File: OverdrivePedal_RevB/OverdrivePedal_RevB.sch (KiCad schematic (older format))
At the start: 18 parts, among them J1 AudioJack2, J2 Barrel_Jack, J3 Conn_01x03, J5 Conn_01x03, J6 AudioJack2, U2 TL071

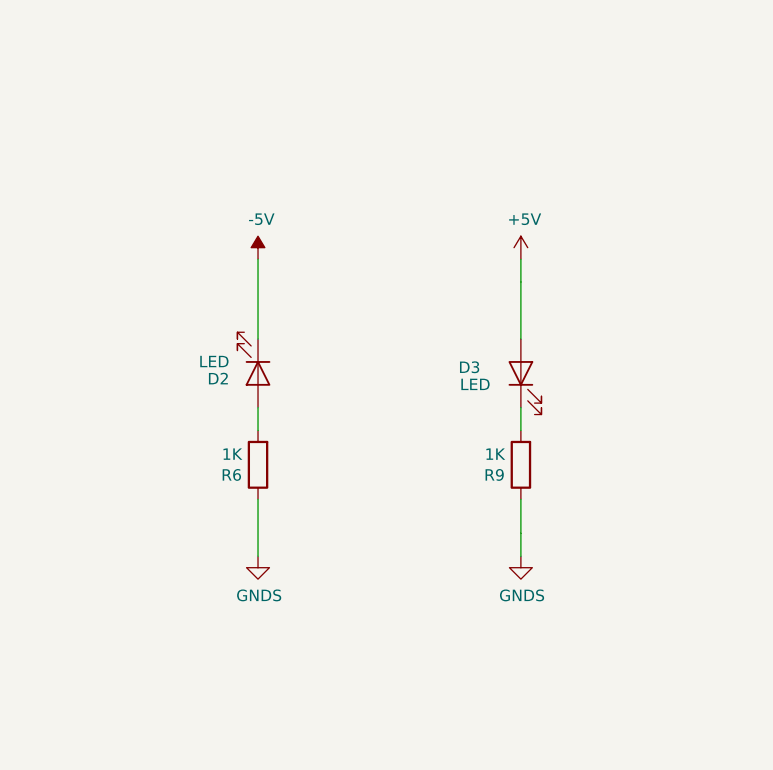
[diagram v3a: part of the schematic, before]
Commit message: Added extra leds
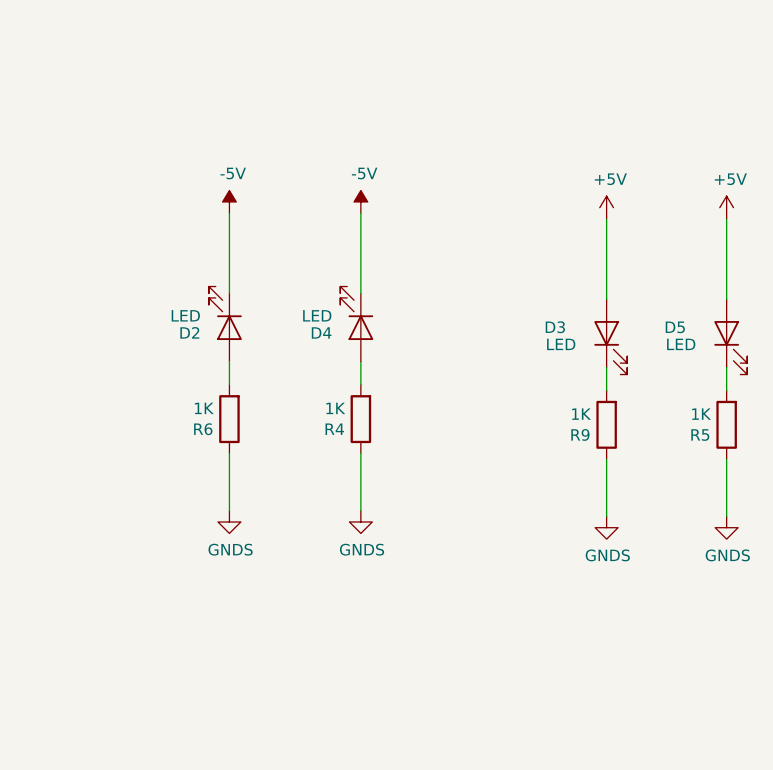
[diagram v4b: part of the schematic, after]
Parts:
- added D4, D5: LED, LED_SMD:LED_1206_3216Metric_Pad1.42x1.75mm_HandSolder, symbol Device:LED
- added R4, R5: 1K, Resistor_SMD:R_0805_2012Metric_Pad1.15x1.40mm_HandSolder, symbol Device:R
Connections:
- wire segments 61 -> 65
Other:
- moved on the sheet: D2, D3, R6, R9
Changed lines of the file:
@@
 L Device:R R9
 U 1 1 5E7266E9
-P 13550 8650
-F 0 "R9" H 13620 8696 50  0000 L CNN
-F 1 "1K" H 13620 8605 50  0000 L CNN
-F 2 "Resistor_SMD:R_0805_2012Metric_Pad1.15x1.40mm_HandSolder" V 13480 8650 50  0001 C CNN
-F 3 "~" H 13550 8650 50  0001 C CNN
-	1    13550 8650
+P 13925 8475
+F 0 "R9" H 13995 8521 50  0000 L CNN
+F 1 "1K" H 13995 8430 50  0000 L CNN
+F 2 "Resistor_SMD:R_0805_2012Metric_Pad1.15x1.40mm_HandSolder" V 13855 8475 50  0001 C CNN
+F 3 "~" H 13925 8475 50  0001 C CNN
+	1    13925 8475
 	-1   0    0    1
 $EndComp
@@
 L Device:R R6
 U 1 1 5E727E16
-P 12400 8650
-F 0 "R6" H 12470 8696 50  0000 L CNN
-F 1 "1K" H 12470 8605 50  0000 L CNN
-F 2 "Resistor_SMD:R_0805_2012Metric_Pad1.15x1.40mm_HandSolder" V 12330 8650 50  0001 C CNN
-F 3 "~" H 12400 8650 50  0001 C CNN
-	1    12400 8650
-	-1   0    0    1
-$EndComp
-Wire Wire Line
-	13550 8500 13550 8400
-Wire Wire Line
-	12400 8500 12400 8400
-Wire Wire Line
-	13550 8100 13550 7850
-Wire Wire Line
-	12400 8100 12400 7750
+P 12275 8450
+F 0 "R6" H 12345 8496 50  0000 L CNN
+F 1 "1K" H 12345 8405 50  0000 L CNN
+F 2 "Resistor_SMD:R_0805_2012Metric_Pad1.15x1.40mm_HandSolder" V 12205 8450 50  0001 C CNN
+F 3 "~" H 12275 8450 50  0001 C CNN
+	1    12275 8450
+	-1   0    0    1
+$EndComp
+Wire Wire Line
+	13925 8325 13925 8225
+Wire Wire Line
+	12275 8300 12275 8200
+Wire Wire Line
+	12275 7900 12275 7550
 $Comp
 L power:GNDS #PWR0108
 U 1 1 5E73B1FE
-P 13550 9050
-F 0 "#PWR0108" H 13550 8800 50  0001 C CNN
-F 1 "GNDS" H 13555 8877 50  0000 C CNN
-F 2 "" H 13550 9050 50  0001 C CNN
-F 3 "" H 13550 9050 50  0001 C CNN
-	1    13550 9050
+P 13925 8875
+F 0 "#PWR0108" H 13925 8625 50  0001 C CNN
+F 1 "GNDS" H 13930 8702 50  0000 C CNN
+F 2 "" H 13925 8875 50  0001 C CNN
+F 3 "" H 13925 8875 50  0001 C CNN
+	1    13925 8875
 	1    0    0    -1
 $EndComp
@@
 L power:+5V #PWR0109
 U 1 1 5E73B611
-P 13550 7750
-F 0 "#PWR0109" H 13550 7600 50  0001 C CNN
-F 1 "+5V" H 13565 7923 50  0000 C CNN
-F 2 "" H 13550 7750 50  0001 C CNN
-F 3 "" H 13550 7750 50  0001 C CNN
-	1    13550 7750
-	1    0    0    -1
-$EndComp
-Wire Wire Line
-	13550 9050 13550 8950
-Wire Wire Line
-	13550 8950 13550 8800
-Wire Wire Line
-	12400 9050 12400 8800
-Wire Wire Line
-	13550 7750 13550 7850
+P 13925 7575
+F 0 "#PWR0109" H 13925 7425 50  0001 C CNN
+F 1 "+5V" H 13940 7748 50  0000 C CNN
+F 2 "" H 13925 7575 50  0001 C CNN
+F 3 "" H 13925 7575 50  0001 C CNN
+	1    13925 7575
+	1    0    0    -1
+$EndComp
+Wire Wire Line
+	12275 8850 12275 8600
 $Comp
 L Connector:AudioJack2 J1
@@
 L Device:LED D2
 U 1 1 5EFC7770
-P 12400 8250
-F 0 "D2" V 12425 8125 50  0000 R CNN
-F 1 "LED" V 12350 8125 50  0000 R CNN
-F 2 "LED_SMD:LED_1206_3216Metric_Pad1.42x1.75mm_HandSolder" H 12400 8250 50  0001 C CNN
-F 3 "~" H 12400 8250 50  0001 C CNN
-	1    12400 8250
+P 12275 8050
+F 0 "D2" V 12300 7925 50  0000 R CNN
+F 1 "LED" V 12225 7925 50  0000 R CNN
+F 2 "LED_SMD:LED_1206_3216Metric_Pad1.42x1.75mm_HandSolder" H 12275 8050 50  0001 C CNN
+F 3 "~" H 12275 8050 50  0001 C CNN
+	1    12275 8050
 	0    1    1    0
 $EndComp
@@
 L Device:LED D3
 U 1 1 5EFC98F4
-P 13550 8250
-F 0 "D3" V 13575 8475 50  0000 C CNN
-F 1 "LED" V 13500 8450 50  0000 C CNN
-F 2 "LED_SMD:LED_1206_3216Metric_Pad1.42x1.75mm_HandSolder" H 13550 8250 50  0001 C CNN
-F 3 "~" H 13550 8250 50  0001 C CNN
-	1    13550 8250
+P 13925 8075
+F 0 "D3" V 13950 8300 50  0000 C CNN
+F 1 "LED" V 13875 8275 50  0000 C CNN
+F 2 "LED_SMD:LED_1206_3216Metric_Pad1.42x1.75mm_HandSolder" H 13925 8075 50  0001 C CNN
+F 3 "~" H 13925 8075 50  0001 C CNN
+	1    13925 8075
 	0    -1   -1   0
 $EndComp
@@
 L power:-5V #PWR0110
 U 1 1 5EFE78DE
-P 12400 7750
-F 0 "#PWR0110" H 12400 7850 50  0001 C CNN
-F 1 "-5V" H 12415 7923 50  0000 C CNN
-F 2 "" H 12400 7750 50  0001 C CNN
-F 3 "" H 12400 7750 50  0001 C CNN
-	1    12400 7750
+P 12275 7550
+F 0 "#PWR0110" H 12275 7650 50  0001 C CNN
+F 1 "-5V" H 12290 7723 50  0000 C CNN
+F 2 "" H 12275 7550 50  0001 C CNN
+F 3 "" H 12275 7550 50  0001 C CNN
+	1    12275 7550
 	1    0    0    -1
 $EndComp
@@
 L power:GNDS #PWR0111
 U 1 1 5EFE9272
-P 12400 9050
-F 0 "#PWR0111" H 12400 8800 50  0001 C CNN
-F 1 "GNDS" H 12405 8877 50  0000 C CNN
-F 2 "" H 12400 9050 50  0001 C CNN
-F 3 "" H 12400 9050 50  0001 C CNN
-	1    12400 9050
-	1    0    0    -1
-$EndComp
+P 12275 8850
+F 0 "#PWR0111" H 12275 8600 50  0001 C CNN
+F 1 "GNDS" H 12280 8677 50  0000 C CNN
+F 2 "" H 12275 8850 50  0001 C CNN
+F 3 "" H 12275 8850 50  0001 C CNN
+	1    12275 8850
+	1    0    0    -1
+$EndComp
+$Comp
+L Device:R R5
+U 1 1 5F01A295
+P 14450 8475
+F 0 "R5" H 14520 8521 50  0000 L CNN
+F 1 "1K" H 14520 8430 50  0000 L CNN
+F 2 "Resistor_SMD:R_0805_2012Metric_Pad1.15x1.40mm_HandSolder" V 14380 8475 50  0001 C CNN
+F 3 "~" H 14450 8475 50  0001 C CNN
+	1    14450 8475
+	-1   0    0    1
+$EndComp
+$Comp
+L Device:R R4
+U 1 1 5F01A29F
+P 12850 8450
+F 0 "R4" H 12920 8496 50  0000 L CNN
+F 1 "1K" H 12920 8405 50  0000 L CNN
+F 2 "Resistor_SMD:R_0805_2012Metric_Pad1.15x1.40mm_HandSolder" V 12780 8450 50  0001 C CNN
+F 3 "~" H 12850 8450 50  0001 C CNN
+	1    12850 8450
+	-1   0    0    1
+$EndComp
+Wire Wire Line
+	14450 8325 14450 8225
+Wire Wire Line
+	12850 8300 12850 8200
+Wire Wire Line
+	12850 7900 12850 7550
+$Comp
+L power:GNDS #PWR015
+U 1 1 5F01A2AD
+P 14450 8875
+F 0 "#PWR015" H 14450 8625 50  0001 C CNN
+F 1 "GNDS" H 14455 8702 50  0000 C CNN
+F 2 "" H 14450 8875 50  0001 C CNN
+F 3 "" H 14450 8875 50  0001 C CNN
+	1    14450 8875
+	1    0    0    -1
+$EndComp
+$Comp
+L power:+5V #PWR013
+U 1 1 5F01A2B7
+P 14450 7575
+F 0 "#PWR013" H 14450 7425 50  0001 C CNN
+F 1 "+5V" H 14465 7748 50  0000 C CNN
+F 2 "" H 14450 7575 50  0001 C CNN
+F 3 "" H 14450 7575 50  0001 C CNN
+	1    14450 7575
+	1    0    0    -1
+$EndComp
+Wire Wire Line
+	12850 8850 12850 8600
+$Comp
+L Device:LED D4
+U 1 1 5F01A2C5
+P 12850 8050
+F 0 "D4" V 12875 7925 50  0000 R CNN
+F 1 "LED" V 12800 7925 50  0000 R CNN
+F 2 "LED_SMD:LED_1206_3216Metric_Pad1.42x1.75mm_HandSolder" H 12850 8050 50  0001 C CNN
+F 3 "~" H 12850 8050 50  0001 C CNN
+	1    12850 8050
+	0    1    1    0
+$EndComp
+$Comp
+L Device:LED D5
+U 1 1 5F01A2CF
+P 14450 8075
+F 0 "D5" V 14475 8300 50  0000 C CNN
+F 1 "LED" V 14400 8275 50  0000 C CNN
+F 2 "LED_SMD:LED_1206_3216Metric_Pad1.42x1.75mm_HandSolder" H 14450 8075 50  0001 C CNN
+F 3 "~" H 14450 8075 50  0001 C CNN
+	1    14450 8075
+	0    -1   -1   0
+$EndComp
+$Comp
+L power:-5V #PWR01
+U 1 1 5F01A2D9
+P 12850 7550
+F 0 "#PWR01" H 12850 7650 50  0001 C CNN
+F 1 "-5V" H 12865 7723 50  0000 C CNN
+F 2 "" H 12850 7550 50  0001 C CNN
+F 3 "" H 12850 7550 50  0001 C CNN
+	1    12850 7550
+	1    0    0    -1
+$EndComp
+$Comp
+L power:GNDS #PWR012
+U 1 1 5F01A2E3
+P 12850 8850
+F 0 "#PWR012" H 12850 8600 50  0001 C CNN
+F 1 "GNDS" H 12855 8677 50  0000 C CNN
+F 2 "" H 12850 8850 50  0001 C CNN
+F 3 "" H 12850 8850 50  0001 C CNN
+	1    12850 8850
+	1    0    0    -1
+$EndComp
+Wire Wire Line
+	13925 7575 13925 7925
+Wire Wire Line
+	13925 8625 13925 8875
+Wire Wire Line
+	14450 7575 14450 7925
+Wire Wire Line
+	14450 8625 14450 8875
 $EndSCHEMATC

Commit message: updated revb design
- Added solidstate ICs for bypass switching to allow for mom. footswitch
- Added STM32L011 MCU
-  Added SE82XX (SOT23) LDOs for 5V and 3V3 rails
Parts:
- removed D4: LED, LED_SMD:LED_1206_3216Metric_Pad1.42x1.75mm_HandSolder, symbol Device:LED
- removed J3, J5: Conn_01x03, Connector_PinHeader_2.54mm:PinHeader_1x03_P2.54mm_Vertical, symbol Connector_Generic:Conn_01x03
- added C6: 100nF, Capacitor_SMD:C_0805_2012Metric_Pad1.15x1.40mm_HandSolder, symbol Device:C
- added J3: Conn_01x05, Connector_PinSocket_2.54mm:PinSocket_1x05_P2.54mm_Vertical, symbol Connector_Generic:Conn_01x05
- added JP1: Jumper_3_Bridged12, Jumper:SolderJumper-3_P1.3mm_Bridged12_Pad1.0x1.5mm, symbol Jumper:Jumper_3_Bridged12
- added SW_FOOT1: SW_SPST, Connector_PinSocket_2.54mm:PinSocket_1x02_P2.54mm_Vertical, symbol Switch:SW_SPST
- added SW_RST1: SW_SPST, Button_Switch_SMD:SW_SPST_CK_KXT3, symbol Switch:SW_SPST
- added U1, U4, U6: DG468DV_T1_E3, Package_SO:TSOP-6_1.65x3.05mm_P0.95mm, symbol DG46x:DG468DV_T1_E3
- added U5: STM32L011D4Px, Package_SO:TSSOP-14_4.4x5mm_P0.65mm, symbol MCU_ST_STM32L0:STM32L011D4Px
- R4: value 1K -> 220R
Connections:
- net labels added: +3V3, BYPASS_ENABLE, FX_ENABLE, GPIO_EXTI4_BYPASS, SYS_NRST, SYS_SWCLK, SYS_SWDIO, TIM2_CH1_PWM, TIM2_CH2_PWM, TIM2_CH3_PWM
- wire segments 65 -> 111
- no-connect marks 2 -> 4
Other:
- note removed: "1 Half DPDT FootSwitch"
- moved on the sheet: C1, C2, C7, C9, D3, D5, J1, J2, J6, R1, R2, R3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

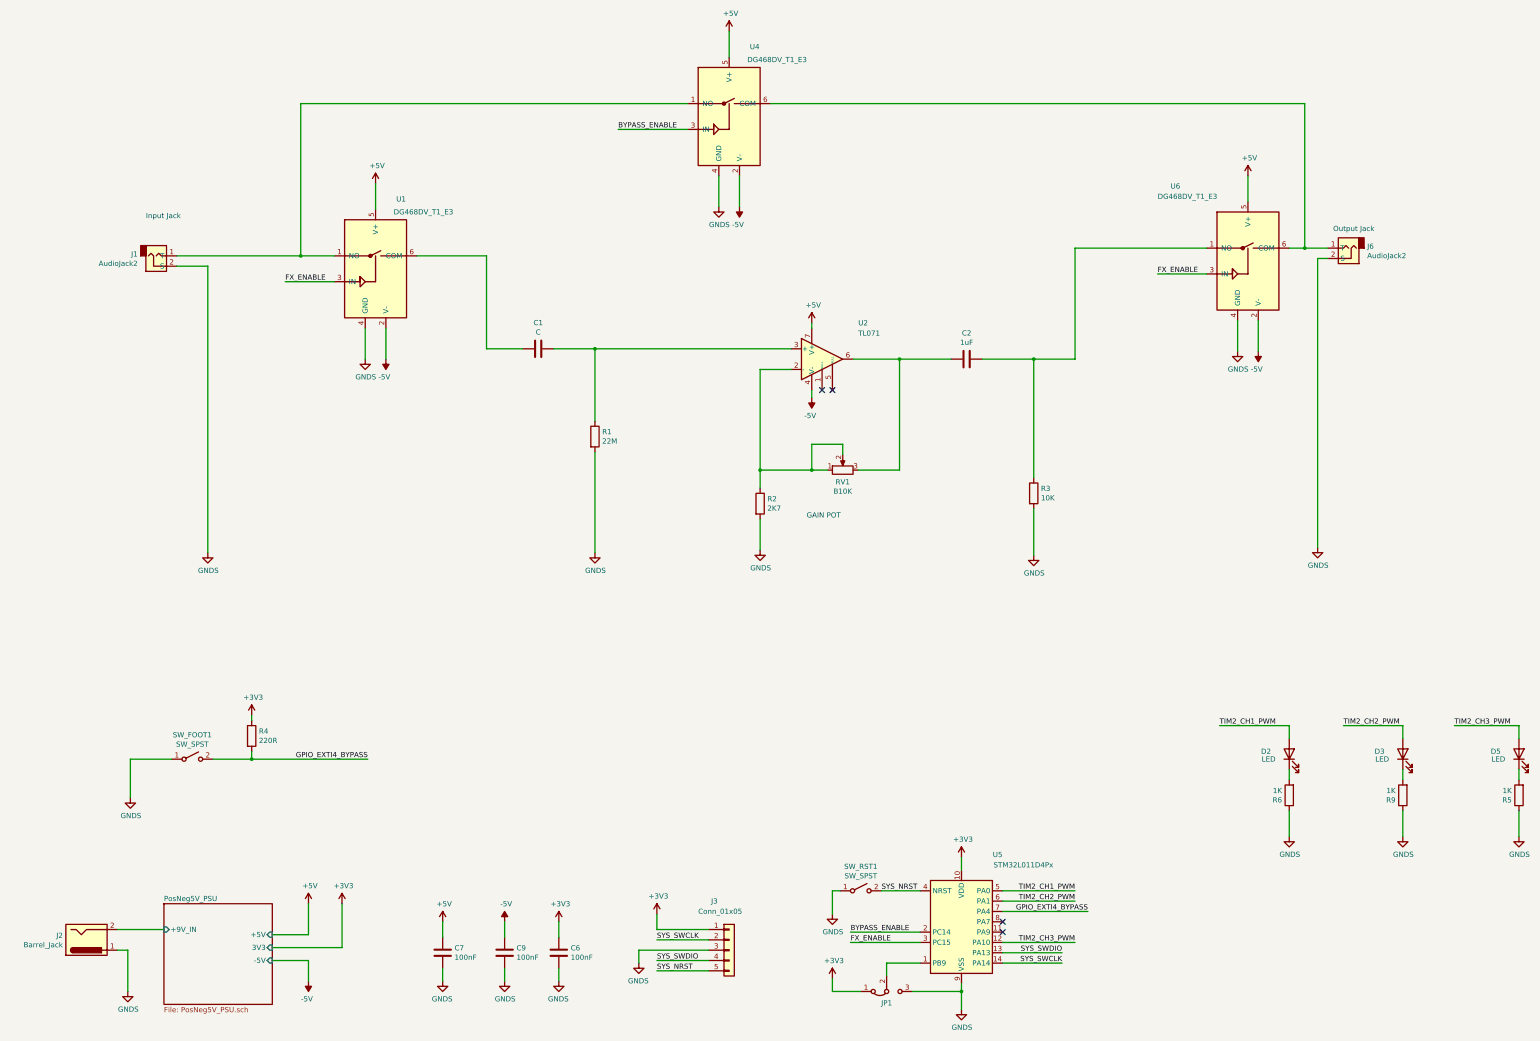
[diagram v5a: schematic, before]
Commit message: Draft layout completed
RevB layout
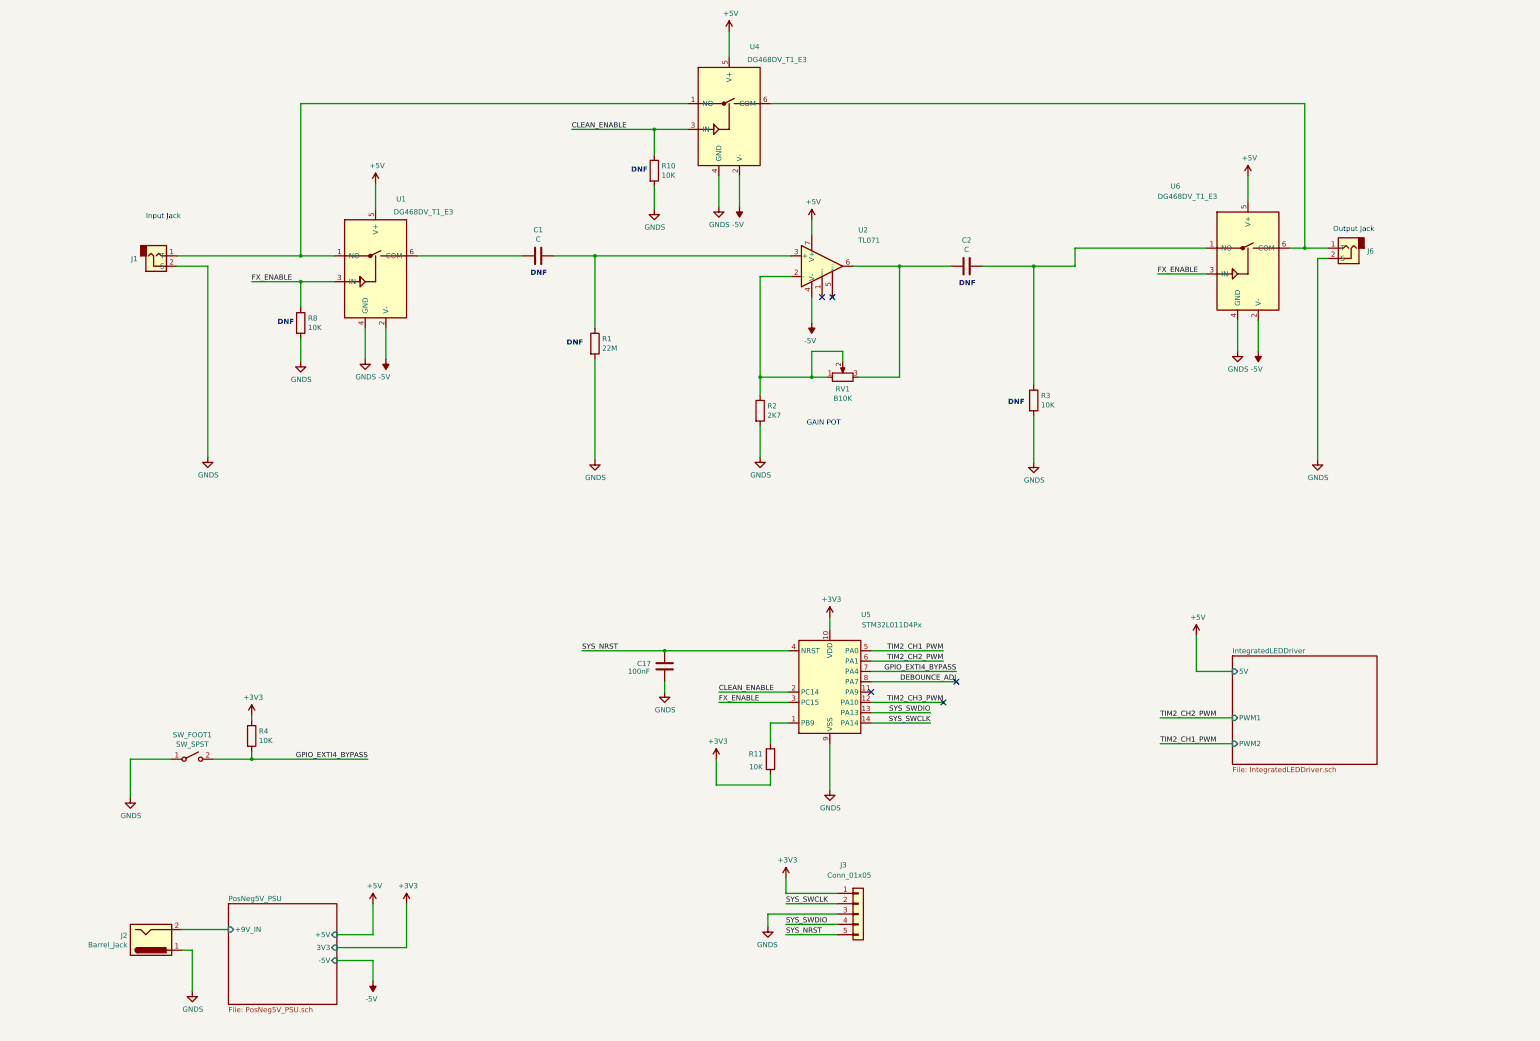
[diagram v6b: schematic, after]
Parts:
- removed C6, C7, C9: 100nF, Capacitor_SMD:C_0805_2012Metric_Pad1.15x1.40mm_HandSolder, symbol Device:C
- removed D2, D3, D5: LED, LED_SMD:LED_1206_3216Metric_Pad1.42x1.75mm_HandSolder, symbol Device:LED
- removed J1, J6: AudioJack2, Connector_PinHeader_2.54mm:PinHeader_1x02_P2.54mm_Vertical, symbol Connector:AudioJack2
- removed JP1: Jumper_3_Bridged12, Jumper:SolderJumper-3_P1.3mm_Bridged12_Pad1.0x1.5mm, symbol Jumper:Jumper_3_Bridged12
- removed R5, R6, R9: 1K, Resistor_SMD:R_0805_2012Metric_Pad1.15x1.40mm_HandSolder, symbol Device:R
- removed SW_RST1: SW_SPST, Button_Switch_SMD:SW_SPST_CK_KXT3, symbol Switch:SW_SPST
- added C17: 100nF, Capacitor_SMD:C_0402_1005Metric, symbol Device:C
- added J1, J6: AudioJack2-Connector, Connector_PinSocket_2.54mm:PinSocket_1x02_P2.54mm_Vertical, symbol audiojack2-connector_numbered:AudioJack2-Connector
- added R10, R11, R8: 10K, Resistor_SMD:R_0402_1005Metric, symbol Device:R
- C1: footprint Capacitor_SMD:C_0805_2012Metric_Pad1.15x1.40mm_HandSolder -> Capacitor_SMD:C_0402_1005Metric
- C2: value 1uF -> C; footprint Capacitor_SMD:C_0805_2012Metric_Pad1.15x1.40mm_HandSolder -> Capacitor_SMD:C_0402_1005Metric
- R1, R2, R3: footprint Resistor_SMD:R_0805_2012Metric_Pad1.15x1.40mm_HandSolder -> Resistor_SMD:R_0402_1005Metric
- R4: value 220R -> 10K; footprint Resistor_SMD:R_0805_2012Metric_Pad1.15x1.40mm_HandSolder -> Resistor_SMD:R_0402_1005Metric
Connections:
- net +3V3: now also R11.1
- net FX_ENABLE: now also R8.1
- net GNDS: now also C17.1, J1.2 (S), J6.2 (S), R10.2, R8.2
- net SYS_NRST: now also C17.2
- net at U1.1 (NO), U4.1 (NO): now also J1.1 (T)
- net at U4.6 (COM), U6.6 (COM): now also J6.1 (T)
- net at U5.1 (PB9): now also R11.2
- net DEBOUNCE_ADJ: now reaches U5.8 (PA7)
- net BYPASS_ENABLE renamed CLEAN_ENABLE
- net CLEAN_ENABLE: now also R10.1
- no-connect marks 4 -> 5
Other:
- note added: "DNF"
- moved on the sheet: C1, C2, J2, J3, R1, R2, R3, RV1, U2, U5
